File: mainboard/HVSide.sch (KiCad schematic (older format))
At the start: 66 parts, among them J11 CONN_2X2, J17 HV, J18 CONN_1X2, J19 CONN_1X2, J4 CONN_2X2, U10 DCDC_ISO_5V_ISO, U15 CD4082, U16 ADCMP350, U19 TCMT1103, U23 CD4072BPW, U24 LM358, U26 TCMT1103, U27 DCDC_ISO_5V, U28 MIC5365-3.3YC5, U29 Si8900, U30 MAX14878AWA+, U7 ADCMP354

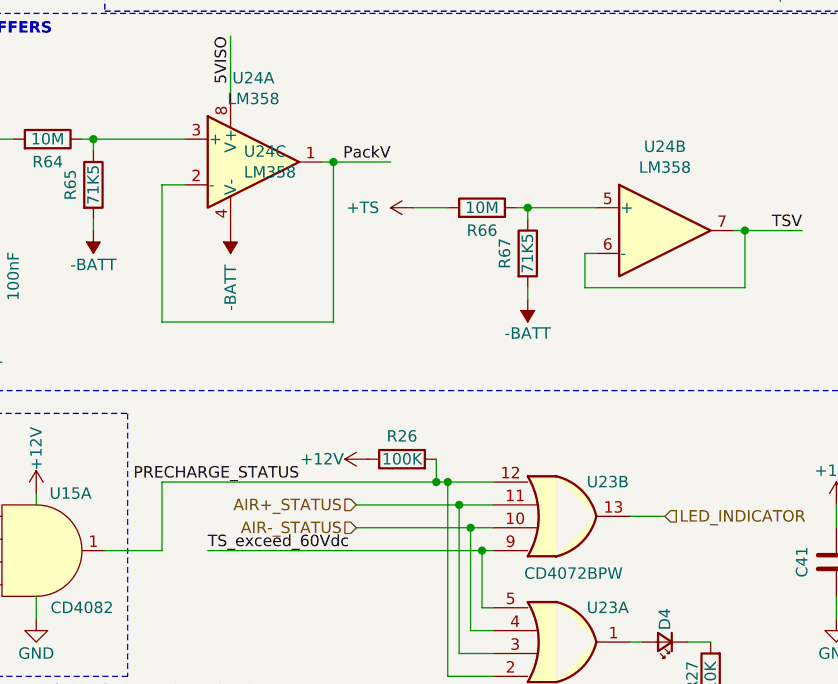
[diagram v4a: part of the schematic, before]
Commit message: adding testpoints
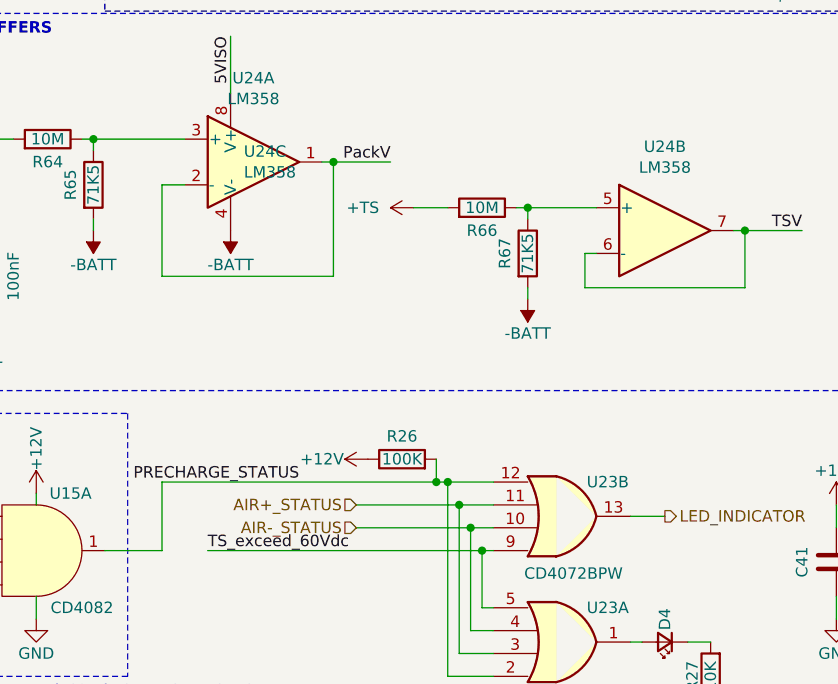
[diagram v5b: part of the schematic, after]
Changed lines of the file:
@@
 P 7450 4300
 F 0 "#PWR0201" H 7450 4150 50  0001 C CNN
-F 1 "-BATT" V 7450 4550 50  0000 C CNN
+F 1 "-BATT" H 7450 4450 50  0000 C CNN
 F 2 "" H 7450 4300 50  0001 C CNN
 F 3 "" H 7450 4300 50  0001 C CNN
@@
 Text HLabel 8000 5500 0    50   Input ~ 0
 AIR+_STATUS
-Text HLabel 9350 5550 2    50   Input ~ 0
+Text HLabel 9350 5550 2    50   Output ~ 0
 LED_INDICATOR
 Text Label 7350 5700 0    50   ~ 0
@@
 $EndComp
 Wire Wire Line
-	7900 4000 7900 4700
-Wire Wire Line
-	7900 4700 7150 4700
-Wire Wire Line
-	7150 4700 7150 4100
+	7900 4000 7900 4500
+Wire Wire Line
+	7900 4500 7150 4500
+Wire Wire Line
+	7150 4500 7150 4100
 Connection ~ 7900 4000
 Wire Wire Line

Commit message: minor changes
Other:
- moved on the sheet: C26, R21, R24, R56, R57, TP?, U19, U7

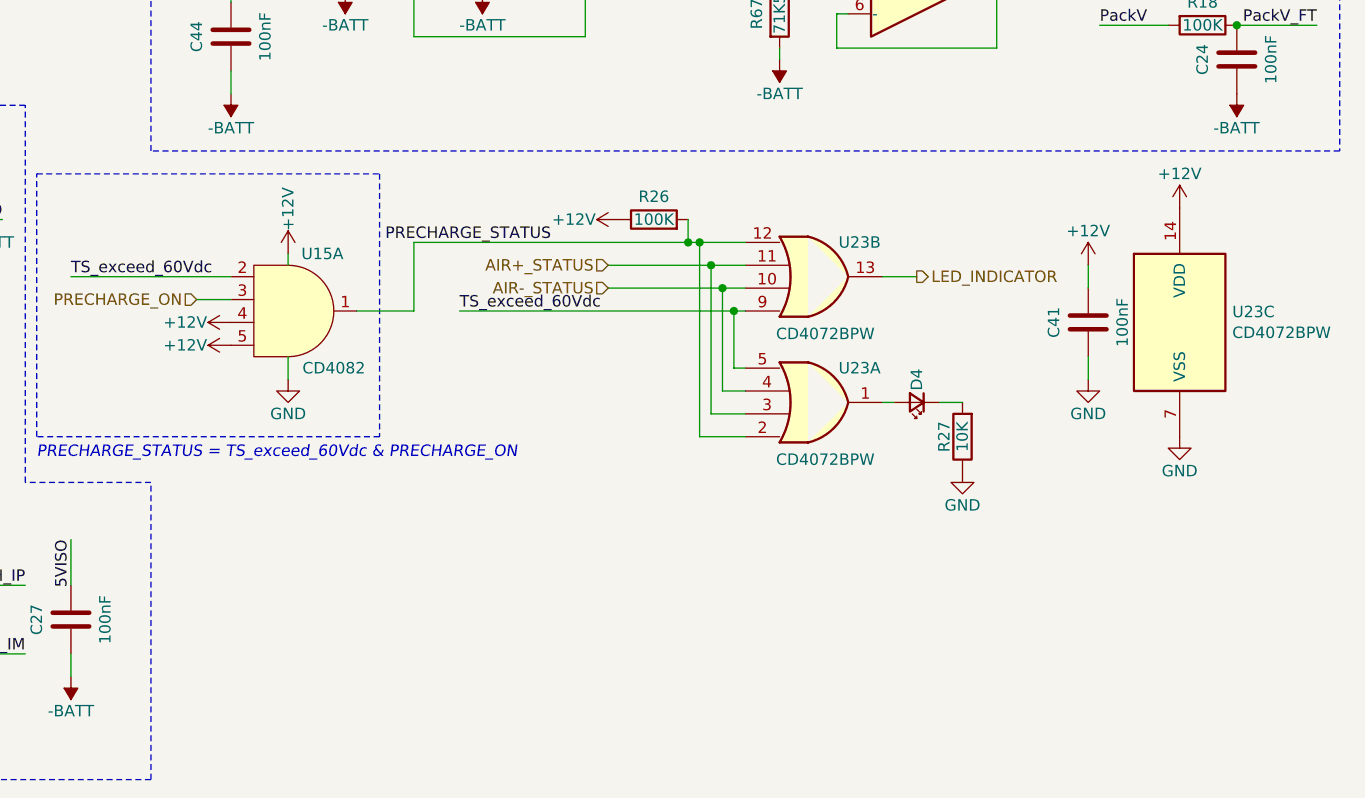
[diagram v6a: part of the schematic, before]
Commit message: Redone the CD4072, it can't light a LED as per datasheet
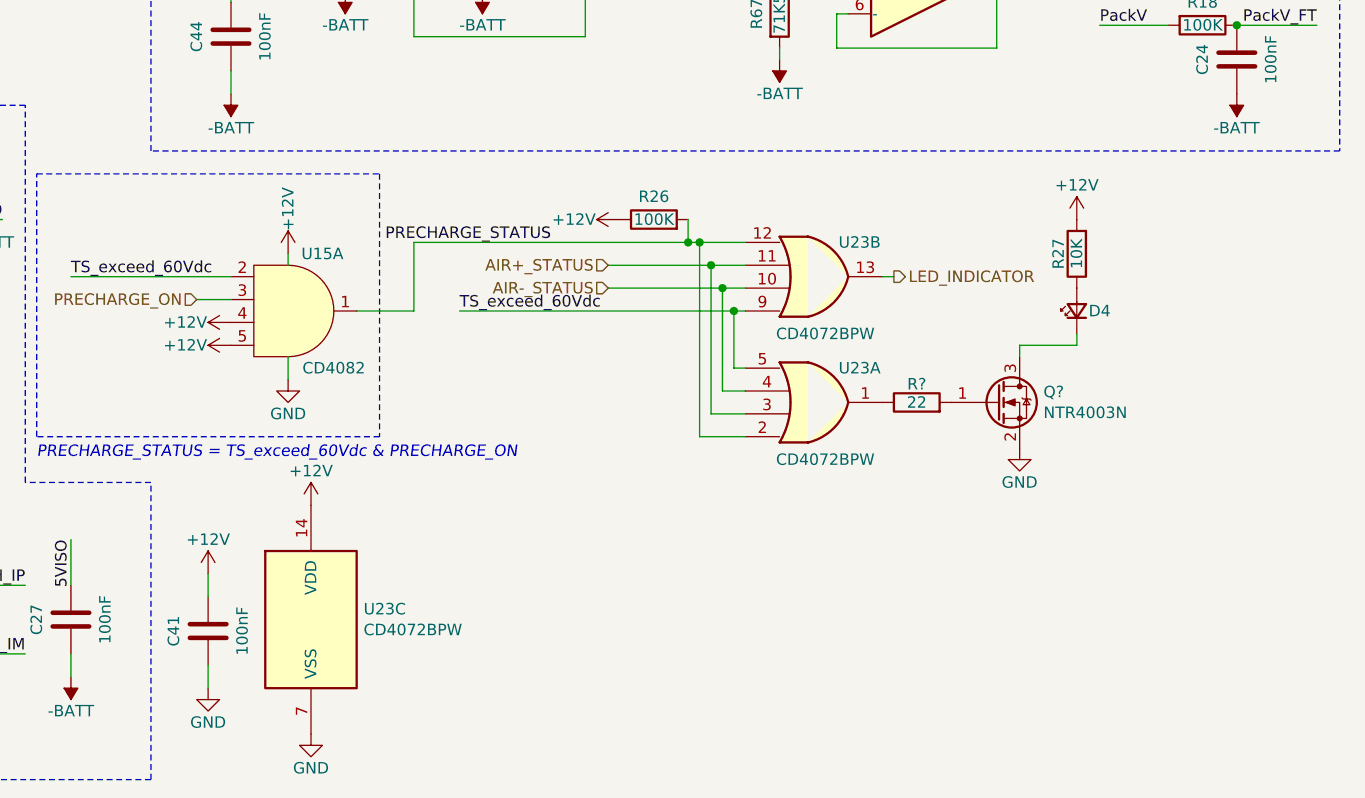
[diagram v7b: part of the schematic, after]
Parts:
- added Q?: NTR4003N, Package_TO_SOT_SMD:SOT-23, symbol Device:Q_NMOS_GSD
- added R?: 22, Resistor_SMD:R_0603_1608Metric, symbol Device:R
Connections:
- net +12V: now also R27.2
- net GND: now also Q?.2 (S); no longer R27.1
- net at U23.1: now also R?.1; no longer D4.2 (A)
- net at D4.1 (K): now also Q?.3 (D); no longer R27.2
- new net: D4.2 (A), R27.1
- new net: Q?.1 (G), R?.2
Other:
- moved on the sheet: C41, D4, R27, U23C
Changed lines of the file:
@@
 	6900 2090 11185 2090
-$Comp
-L 4xxx:4072 U23
-U 3 1 5DEE756A
-P 10500 5750
-F 0 "U23" H 10730 5796 50  0000 L CNN
-F 1 "CD4072BPW" H 10730 5705 50  0000 L CNN
-F 2 "Package_SO:TSSOP-14_4.4x5mm_P0.65mm" H 10500 5750 50  0001 C CNN
-F 3 "http://www.intersil.com/content/dam/Intersil/documents/cd40/cd4071bms-72bms-75bms.pdf" H 10500 5750 50  0001 C CNN
-F 4 "https://www.mouser.it/ProductDetail/Texas-Instruments/CD4072BPW?qs=HTr%252BoA4jRild%2FUl27Cy93g%3D%3D" H 10500 5750 50  0001 C CNN "Mouser"
-	3    10500 5750
-	1    0    0    -1
-$EndComp
-$Comp
-L power:GND #PWR0214
-U 1 1 5DEF1B3F
-P 10500 6250
-F 0 "#PWR0214" H 10500 6000 50  0001 C CNN
-F 1 "GND" H 10500 6100 50  0000 C CNN
-F 2 "" H 10500 6250 50  0001 C CNN
-F 3 "" H 10500 6250 50  0001 C CNN
-	1    10500 6250
-	1    0    0    -1
-$EndComp
 $Comp
 L Connector_Generic:Conn_02x02_Odd_Even J17
@@
 $EndComp
 Wire Wire Line
-	10100 5900 10100 6000
-Wire Wire Line
-	10100 5500 10100 5600
-$Comp
-L Device:C C41
-U 1 1 5DE9D4DB
-P 10100 5750
-F 0 "C41" V 9950 5750 50  0000 C CNN
-F 1 "100nF" V 10250 5750 50  0000 C CNN
-F 2 "Capacitor_SMD:C_0603_1608Metric" H 10138 5600 50  0001 C CNN
-F 3 "~" H 10100 5750 50  0001 C CNN
-	1    10100 5750
-	1    0    0    -1
-$EndComp
-$Comp
-L power:+12V #PWR?
-U 1 1 5DE9D4D5
-P 10100 5500
-AR Path="/5DE9D4D5" Ref="#PWR?"  Part="1"
-AR Path="/5B50ED38/5DE9D4D5" Ref="#PWR0207"  Part="1"
-F 0 "#PWR0207" H 10100 5350 50  0001 C CNN
-F 1 "+12V" H 10100 5650 50  0000 C CNN
-F 2 "" H 10100 5500 50  0001 C CNN
-F 3 "" H 10100 5500 50  0001 C CNN
-	1    10100 5500
-	1    0    0    -1
-$EndComp
-$Comp
-L power:GND #PWR0208
-U 1 1 5DE9D4CF
-P 10100 6000
-F 0 "#PWR0208" H 10100 5750 50  0001 C CNN
-F 1 "GND" H 10100 5850 50  0000 C CNN
-F 2 "" H 10100 6000 50  0001 C CNN
-F 3 "" H 10100 6000 50  0001 C CNN
-	1    10100 6000
-	1    0    0    -1
-$EndComp
-Wire Wire Line
 	5700 650  5600 650
 Wire Wire Line
 	6200 650  6300 650
-$Comp
-L power:+12V #PWR?
-U 1 1 5E20F503
-P 10500 5250
-AR Path="/5E20F503" Ref="#PWR?"  Part="1"
-AR Path="/5B50ED38/5E20F503" Ref="#PWR0213"  Part="1"
-F 0 "#PWR0213" H 10500 5100 50  0001 C CNN
-F 1 "+12V" H 10500 5400 50  0000 C CNN
-F 2 "" H 10500 5250 50  0001 C CNN
-F 3 "" H 10500 5250 50  0001 C CNN
-	1    10500 5250
-	1    0    0    -1
-$EndComp
 $Comp
 L power:-BATT #PWR0176
@@
 Text HLabel 8000 5500 0    50   Input ~ 0
 AIR+_STATUS
-Text HLabel 9350 5550 2    50   Output ~ 0
+Text HLabel 9250 5550 2    50   Output ~ 0
 LED_INDICATOR
 Text Label 7350 5700 0    50   ~ 0
@@
 TS_OVER_60V
 Wire Wire Line
-	9200 5550 9350 5550
+	9200 5550 9250 5550
 Wire Wire Line
 	8150 1300 8200 1300
@@
 	1    0    0    1
 $EndComp
-Wire Wire Line
-	9200 6100 9250 6100
 $Comp
 L MainBoard:4072 U23
@@
 L Device:R R?
 U 1 1 5F653520
-P 9550 6250
+P 10050 5450
 AR Path="/5DE633EC/5F653520" Ref="R?"  Part="1"
 AR Path="/5F653520" Ref="R?"  Part="1"
 AR Path="/5B50ED38/5F653520" Ref="R27"  Part="1"
-F 0 "R27" V 9630 6250 50  0000 C CNN
-F 1 "10K" V 9550 6250 50  0000 C CNN
-F 2 "Resistor_SMD:R_0603_1608Metric" V 9480 6250 50  0001 C CNN
-F 3 "~" H 9550 6250 50  0001 C CNN
-	1    9550 6250
+F 0 "R27" V 10130 5450 50  0000 C CNN
+F 1 "10K" V 10050 5450 50  0000 C CNN
+F 2 "Resistor_SMD:R_0603_1608Metric" V 9980 5450 50  0001 C CNN
+F 3 "~" H 10050 5450 50  0001 C CNN
+	1    10050 5450
 	-1   0    0    1
-$EndComp
-$Comp
-L power:GND #PWR?
-U 1 1 5F653527
-P 9550 6400
-AR Path="/5F653527" Ref="#PWR?"  Part="1"
-AR Path="/5B50ED38/5F653527" Ref="#PWR03"  Part="1"
-F 0 "#PWR03" H 9550 6150 50  0001 C CNN
-F 1 "GND" H 9550 6250 50  0000 C CNN
-F 2 "" H 9550 6400 50  0001 C CNN
-F 3 "" H 9550 6400 50  0001 C CNN
-	1    9550 6400
-	1    0    0    -1
 $EndComp
 $Comp
 L Device:LED_Small D?
 U 1 1 5F65351A
-P 9350 6100
+P 10050 5700
 AR Path="/5DE633EC/5F65351A" Ref="D?"  Part="1"
 AR Path="/5F65351A" Ref="D?"  Part="1"
 AR Path="/5B50ED38/5F65351A" Ref="D4"  Part="1"
-F 0 "D4" V 9350 6000 50  0000 C CNN
-F 1 "LED_Small" H 9350 6244 50  0001 C CNN
-F 2 "LED_SMD:LED_0603_1608Metric_Castellated" V 9350 6100 50  0001 C CNN
-F 3 "~" V 9350 6100 50  0001 C CNN
-	1    9350 6100
-	-1   0    0    1
-$EndComp
-Wire Wire Line
-	9450 6100 9550 6100
+F 0 "D4" V 10050 5600 50  0000 C CNN
+F 1 "LED_Small" H 10050 5844 50  0001 C CNN
+F 2 "LED_SMD:LED_0603_1608Metric_Castellated" V 10050 5700 50  0001 C CNN
+F 3 "~" V 10050 5700 50  0001 C CNN
+	1    10050 5700
+	0    -1   -1   0
+$EndComp
 $Comp
 L Device:R R29
@@
 Wire Wire Line
 	1250 2800 1800 2800
+$Comp
+L Device:Q_NMOS_GSD Q?
+U 1 1 60503C80
+P 9700 6100
+AR Path="/5B045B0D/60503C80" Ref="Q?"  Part="1"
+AR Path="/5B50ED38/60503C80" Ref="Q?"  Part="1"
+F 0 "Q?" H 9904 6146 50  0000 L CNN
+F 1 "NTR4003N" H 9904 6055 50  0000 L CNN
+F 2 "Package_TO_SOT_SMD:SOT-23" H 9900 6200 50  0001 C CNN
+F 3 "https://www.mouser.it/ProductDetail/Toshiba/SSM3K361TULF?qs=sGAEpiMZZMshyDBzk1%2FWi%2FD7Em5shE8qqtsfXGfVhuGHqmGZGu2Z8A%3D%3D" H 9700 6100 50  0001 C CNN
+	1    9700 6100
+	1    0    0    -1
+$EndComp
+$Comp
+L Device:R R?
+U 1 1 60519B24
+P 9350 6100
+AR Path="/5DE633EC/60519B24" Ref="R?"  Part="1"
+AR Path="/60519B24" Ref="R?"  Part="1"
+AR Path="/5B50ED38/60519B24" Ref="R?"  Part="1"
+F 0 "R?" V 9430 6100 50  0000 C CNN
+F 1 "22" V 9350 6100 50  0000 C CNN
+F 2 "Resistor_SMD:R_0603_1608Metric" V 9280 6100 50  0001 C CNN
+F 3 "~" H 9350 6100 50  0001 C CNN
+	1    9350 6100
+	0    -1   -1   0
+$EndComp
+$Comp
+L power:GND #PWR?
+U 1 1 6053D78D
+P 9800 6300
+AR Path="/6053D78D" Ref="#PWR?"  Part="1"
+AR Path="/5B50ED38/6053D78D" Ref="#PWR?"  Part="1"
+F 0 "#PWR?" H 9800 6050 50  0001 C CNN
+F 1 "GND" H 9800 6150 50  0000 C CNN
+F 2 "" H 9800 6300 50  0001 C CNN
+F 3 "" H 9800 6300 50  0001 C CNN
+	1    9800 6300
+	1    0    0    -1
+$EndComp
+Wire Wire Line
+	9800 5900 9800 5850
+Wire Wire Line
+	9800 5850 10050 5850
+Wire Wire Line
+	10050 5850 10050 5800
+$Comp
+L power:+12V #PWR?
+U 1 1 60561AF7
+P 10050 5300
+AR Path="/60561AF7" Ref="#PWR?"  Part="1"
+AR Path="/5B50ED38/60561AF7" Ref="#PWR?"  Part="1"
+F 0 "#PWR?" H 10050 5150 50  0001 C CNN
+F 1 "+12V" H 10050 5450 50  0000 C CNN
+F 2 "" H 10050 5300 50  0001 C CNN
+F 3 "" H 10050 5300 50  0001 C CNN
+	1    10050 5300
+	1    0    0    -1
+$EndComp
+$Comp
+L power:+12V #PWR?
+U 1 1 5E20F503
+P 6700 6550
+AR Path="/5E20F503" Ref="#PWR?"  Part="1"
+AR Path="/5B50ED38/5E20F503" Ref="#PWR0213"  Part="1"
+F 0 "#PWR0213" H 6700 6400 50  0001 C CNN
+F 1 "+12V" H 6700 6700 50  0000 C CNN
+F 2 "" H 6700 6550 50  0001 C CNN
+F 3 "" H 6700 6550 50  0001 C CNN
+	1    6700 6550
+	1    0    0    -1
+$EndComp
+$Comp
+L power:GND #PWR0208
+U 1 1 5DE9D4CF
+P 6250 7350
+F 0 "#PWR0208" H 6250 7100 50  0001 C CNN
+F 1 "GND" H 6250 7200 50  0000 C CNN
+F 2 "" H 6250 7350 50  0001 C CNN
+F 3 "" H 6250 7350 50  0001 C CNN
+	1    6250 7350
+	1    0    0    -1
+$EndComp
+$Comp
+L power:+12V #PWR?
+U 1 1 5DE9D4D5
+P 6250 6850
+AR Path="/5DE9D4D5" Ref="#PWR?"  Part="1"
+AR Path="/5B50ED38/5DE9D4D5" Ref="#PWR0207"  Part="1"
+F 0 "#PWR0207" H 6250 6700 50  0001 C CNN
+F 1 "+12V" H 6250 7000 50  0000 C CNN
+F 2 "" H 6250 6850 50  0001 C CNN
+F 3 "" H 6250 6850 50  0001 C CNN
+	1    6250 6850
+	1    0    0    -1
+$EndComp
+$Comp
+L Device:C C41
+U 1 1 5DE9D4DB
+P 6250 7100
+F 0 "C41" V 6100 7100 50  0000 C CNN
+F 1 "100nF" V 6400 7100 50  0000 C CNN
+F 2 "Capacitor_SMD:C_0603_1608Metric" H 6288 6950 50  0001 C CNN
+F 3 "~" H 6250 7100 50  0001 C CNN
+	1    6250 7100
+	1    0    0    -1
+$EndComp
+Wire Wire Line
+	6250 6850 6250 6950
+Wire Wire Line
+	6250 7250 6250 7350
+$Comp
+L power:GND #PWR0214
+U 1 1 5DEF1B3F
+P 6700 7550
+F 0 "#PWR0214" H 6700 7300 50  0001 C CNN
+F 1 "GND" H 6700 7400 50  0000 C CNN
+F 2 "" H 6700 7550 50  0001 C CNN
+F 3 "" H 6700 7550 50  0001 C CNN
+	1    6700 7550
+	1    0    0    -1
+$EndComp
+$Comp
+L 4xxx:4072 U23
+U 3 1 5DEE756A
+P 6700 7050
+F 0 "U23" H 6930 7096 50  0000 L CNN
+F 1 "CD4072BPW" H 6930 7005 50  0000 L CNN
+F 2 "Package_SO:TSSOP-14_4.4x5mm_P0.65mm" H 6700 7050 50  0001 C CNN
+F 3 "http://www.intersil.com/content/dam/Intersil/documents/cd40/cd4071bms-72bms-75bms.pdf" H 6700 7050 50  0001 C CNN
+F 4 "https://www.mouser.it/ProductDetail/Texas-Instruments/CD4072BPW?qs=HTr%252BoA4jRild%2FUl27Cy93g%3D%3D" H 6700 7050 50  0001 C CNN "Mouser"
+	3    6700 7050
+	1    0    0    -1
+$EndComp
 $EndSCHEMATC

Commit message: v1.1 as printed
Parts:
- removed C? (x3): 100nF, Capacitor_SMD:C_0603_1608Metric, symbol Device:C_Small
- removed J4: CONN_2X2, MainBoard:Molex_Micro-Fit_3.0_43045-0412_2x02_P3.00mm_Vertical, symbol Connector_Generic:Conn_02x02_Counter_Clockwise
- removed Q?: NTR4003N, Package_TO_SOT_SMD:SOT-23, symbol Device:Q_NMOS_GSD
- removed R31, R32, R?: 22, Resistor_SMD:R_0603_1608Metric, symbol Device:R
- removed R69: 2K, Resistor_SMD:R_0603_1608Metric, symbol Device:R
- removed R?: 330K, Resistor_SMD:R_0603_1608Metric, symbol Device:R
- removed R?: 604, Resistor_SMD:R_0603_1608Metric, symbol Device:R
- removed R?: 1K4, Resistor_SMD:R_0603_1608Metric, symbol Device:R
- removed R? (x2): 150, Resistor_SMD:R_0603_1608Metric, symbol Device:R
- removed U10: DCDC_ISO_5V_ISO, MainBoard:DC_DC_ISO_ROExxxx, symbol MainBoard:DCDC_ISO_12V_ISO
- removed U23: CD4072BPW, Package_SO:TSSOP-14_4.4x5mm_P0.65mm, symbol 4xxx:4072
- removed U?: HM2103, MainBoard:HM2103, symbol MainBoard:HM2103
- removed U?: LTC6820, MainBoard:MSOP-16, symbol MainBoard:LTC6820
- added C1, C2, C3: 100nF, Capacitor_SMD:C_0603_1608Metric, symbol Device:C
- added D19, D20: D, MainBoard:SOD_323HE, symbol Device:D
- added D21: 1N4148W, Diode_SMD:D_SOD-123, symbol Diode:1N4148W
- added J4: CONN_2X2, MainBoard:Molex_Micro-Fit_3.0_43045-0612_2x03_P3.00mm_Vertical, symbol Connector_Generic:Conn_02x03_Counter_Clockwise
- added J8: CONN_1X2, MainBoard:Molex_Micro-Fit_3.0_43650-0215_1x02_P3.00mm_Vertical, symbol Connector_Generic:Conn_01x02
- added JP1: prom_select, Jumper:SolderJumper-3_P1.3mm_Open_RoundedPad1.0x1.5mm, symbol Jumper:SolderJumper_3_Open
- added JP6: SolderJumper_3_Open, Jumper:SolderJumper-3_P1.3mm_Open_RoundedPad1.0x1.5mm, symbol Jumper:SolderJumper_3_Open
- added Q1, Q10, Q11, Q12: NTR5105PT1G, Package_TO_SOT_SMD:SOT-23, symbol Device:Q_PMOS_GSD
- added Q4: 2N7002NXAKR, Package_TO_SOT_SMD:SOT-23, symbol Transistor_FET:2N7002
- added R16, R19: 1K, Resistor_SMD:R_0603_1608Metric, symbol Device:R
- added R20, R34: 0, Resistor_SMD:R_0603_1608Metric, symbol Device:R
- added R3: 100K, Resistor_SMD:R_0603_1608Metric, symbol Device:R
- added RN19, RN20, RN21: 22, MainBoard:R_network_4x1_bourns_CAY16, symbol Device:R_Pack04_Split
- added RV1: 10k, Potentiometer_SMD:Potentiometer_Bourns_3314J_Vertical, symbol Device:R_POT
- added TP18: TS_OVER_60V, TestPoint:TestPoint_Pad_D1.0mm, symbol Connector:TestPoint
- added TP19: PC_ST, TestPoint:TestPoint_Pad_D1.0mm, symbol Connector:TestPoint
- added TP31: -BATT, MainBoard:TestPoint_GNDedge, symbol Connector:TestPoint
- added TP38: VS_FT, TestPoint:TestPoint_Pad_D1.0mm, symbol Connector:TestPoint
- added U2: TSC211, Package_TO_SOT_SMD:SOT-363_SC-70-6, symbol MainBoard:TSC21x
- C42: value 6.8uF -> 10uF
- J11: symbol Connector_Generic:Conn_02x02_Counter_Clockwise -> Connector_Generic:Conn_02x02_Odd_Even
- R56, R64, R66: footprint Resistor_SMD:R_1206_3216Metric -> Resistor_SMD:R_2010_5025Metric
- R59: value 1K -> 100
- TP10, TP11, TP12, TP13, TP14: renamed from TP?; footprint (none) -> TestPoint:TestPoint_Pad_D1.0mm
- U30: footprint Package_SO:SOIC-8_7.5x5.85mm_P1.27mm -> Package_SO:SOIC-8W_5.3x5.3mm_P1.27mm
- gave numbers to parts that had none: 1
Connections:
- net +12V: now also Q1.2 (S), Q10.2 (S), Q11.2 (S), Q12.2 (S)
- net -BATT: now also C1.2, C2.1, C3.1, D21.1 (K), J4.5 (Pin_5), JP6.3 (B), TP31.1, U2.2 (GND)
- net 3V3ISO: now also C2.2, JP1.3 (B), R16.2, RV1.3, U2.3 (VCC)
- net 5VISO: now also JP1.1 (A)
- net AIR+_STATUS: now also RN20.2 (R2.1)
- net AIR-_STATUS: now also RN20.3 (R3.1)
- net GND: now also Q4.2 (S)
- net PRECHARGE_STATUS: now also RN20.1 (R1.1), TP19.1
- net PROMINENT+: now also J4.2 (Pin_2)
- net PROMINENT-: now also J4.1 (Pin_1)
- net RX: now also RN19.7 (R2.2)
- net RX_CELL: now also RN19.6 (R3.2); no longer U30.1 (RXD)
- net TS_OVER_60V: now also RN20.4 (R4.1), TP18.1
- net TX: now also RN19.8 (R1.2)
- net TX_CELL: now also RN19.5 (R4.2); no longer U30.2 (TXD)
- net ~RST~_8902: now also R19.1
- net at U29.12 (TX): now also RN19.1 (R1.1)
- net at U29.13 (RX): now also RN19.2 (R2.1)
- net VS_FT: now reaches U29.5 (AIN2)
- net VS_FT: now also C3.2, R3.1, TP38.1
- net at D4.1 (K): now also Q4.3 (D), R20.1
- net 5V_FROM_CELL: no longer names the net of C17.1, R59.1, U16.4 (VCC)
- net 5V_FROM_CELL: now also D19.1 (K), D20.1 (K)
- net ISO_CANH_IP renamed ISO_CANH
- net ISO_CANH: now also J11.2 (Pin_2); no longer J11.1 (Pin_1)
- net ISO_CANL_IM renamed ISO_CANL
- net ISO_CANL: now also J11.1 (Pin_1); no longer J11.2 (Pin_2)
- net si890x_reset renamed SI890x_RESET
- new net: RN19.3 (R3.1), U30.1 (RXD)
- new net: RN19.4 (R4.1), U30.2 (TXD)
- new net: Q4.1 (G), RN21.1 (R1.1)
- new net: Q1.3 (D), Q10.3 (D), Q11.3 (D), Q12.3 (D), R34.1, RN21.8 (R1.2)
- new net: D20.2 (A), JP1.2 (C)
- new net: JP6.2 (C), RV1.1
- new net: Q1.1 (G), RN20.8 (R1.2)
- new net: Q10.1 (G), RN20.7 (R2.2)
- new net: Q11.1 (G), RN20.6 (R3.2)
- new net: Q12.1 (G), RN20.5 (R4.2)
- new net: R16.1, R19.2
- new net 0V5ref: C1.1, D21.2 (A), JP6.1 (A), RV1.2, U2.1 (REF)
- new net CELLBOARD_5V: D19.2 (A), J4.4 (Pin_4)
- new net JUMPER_CELLBOARD: J4.3 (Pin_3), J4.6 (Pin_6)
- new net TSAL: R20.2, R34.2
- new net VS: R3.2, U2.6 (OUT)
- new net VS+: J8.2 (Pin_2), U2.4 (VIN+)
- new net VS-: J8.1 (Pin_1), U2.5 (VIN-)
- no-connect marks 8 -> 5
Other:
- note added: ""IN" connected to the NEGATIVE comparator input\nIN < 0.6V -> OUT Z\nIN > 0.6V -> OUT LOW"
- note added: ""IN" connected to the POSITIVE comparator input\nIN < 0.6V -> OUT LOW\nIN > 0.6V -> OUT Z"
- note added: "DNP"
- note added: "LOW -> Safe, no voltage on TS\nHIGH -> ">60V" on TS or fault"
- note added: "Prominent\nIndicator\n(RED LED 1.5V \n@ 10mA)"
- note added: "R20: place to invert TSAL logic (remove R34 in this case)"
- note added: "Rs=50e-6 Ohm\nThe shunt is connected between -BATT and it's AIR.\nVS- goes to the AIR side\nVS+ goes to the -BATT side\nConnect -BATT and VS+ only on the big cable!"
- note added: "The backup battery can be a 3V coincell (place jumper on 3V3)\n or a normal rechargeable lithium (jumper on 5V)"
- note removed: ""IN" connected to the NEGATIVE comparator input\nINTERNAL Vref=0.6V 1%\nHigh voltage (up to 22 V) tolerance on VIN"
- note removed: ""IN" connected to thePOSITIVE comparator input\nINTERNAL Vref=0.6V 1%\nHigh voltage (up to 22 V) tolerance on VIN"
- note removed: "EXT_POWER&PROMIMENT"
- note removed: "PRECHARGE_STATUS = TS_exceed_60Vdc & PRECHARGE_ON\n"
- note removed: "Prominent\nIndicator\n25mA"
- note removed: "Supply from the first cell to be \nsure the prominent is powered.\nONLY CONNECT THE FIRST CELL\n BECAUSE OF BOARD CLEARANCES"
- note removed: "choose only one between up or down circuits"
- note removed: "isoSPI INTERFACE"
- moved on the sheet: C16, C17, C23, C24, C26, C27, C40, C41, C43, C44, D4, J11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
